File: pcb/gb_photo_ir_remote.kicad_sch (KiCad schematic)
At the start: 10 parts, among them SW1 SW_Push_SPDT, SW2 SW_Push_SPDT, U1 NE555P

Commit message: build
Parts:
- BT1: footprint Battery:BatteryHolder_Keystone_1060_1x2032 -> REB:REB_BatteryHolder_2032
- C1: footprint Capacitor_THT:C_Rect_L9.0mm_W3.4mm_P7.50mm_MKT -> Capacitor_THT:C_Disc_D5.0mm_W2.5mm_P2.50mm
- D1, D2: footprint LED_THT:LED_D5.0mm_Horizontal_O3.81mm_Z3.0mm -> LED_THT:LED_D5.0mm_Horizontal_O1.27mm_Z3.0mm
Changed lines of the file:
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@@
       (effects (font (size 1.27 1.27)) (justify left))
     )
-    (property "Footprint" "Battery:BatteryHolder_Keystone_1060_1x2032" (at 34.29 67.056 90)
+    (property "Footprint" "REB:REB_BatteryHolder_2032" (at 34.29 67.056 90)
       (effects (font (size 1.27 1.27)) hide)
     )
     (property "Datasheet" "~" (at 34.29 67.056 90)
       (effects (font (size 1.27 1.27)) hide)
+    )
+    (property "Notes" "" (at 34.29 68.58 0)
+      (effects (font (size 1.27 1.27)))
     )
     (pin "1")
@@
       (effects (font (size 1.27 1.27)) (justify left))
     )
-    (property "Footprint" "Capacitor_THT:C_Rect_L9.0mm_W3.4mm_P7.50mm_MKT" (at 62.23 88.9 0)
+    (property "Footprint" "Capacitor_THT:C_Disc_D5.0mm_W2.5mm_P2.50mm" (at 62.23 88.9 0)
       (effects (font (size 1.27 1.27)) hide)
     )
@@
       (effects (font (size 1.27 1.27)) hide)
     )
+    (property "Notes" "" (at 62.23 88.9 0)
+      (effects (font (size 1.27 1.27)))
+    )
     (pin "1")
     (pin "2")
@@
       (effects (font (size 1.27 1.27)))
     )
-    (property "Footprint" "LED_THT:LED_D5.0mm_Horizontal_O3.81mm_Z3.0mm" (at 123.19 62.23 0)
+    (property "Footprint" "LED_THT:LED_D5.0mm_Horizontal_O1.27mm_Z3.0mm" (at 123.19 62.23 0)
       (effects (font (size 1.27 1.27)) hide)
     )
@@
       (effects (font (size 1.27 1.27)))
     )
-    (property "Footprint" "LED_THT:LED_D5.0mm_Horizontal_O3.81mm_Z3.0mm" (at 123.19 35.56 0)
+    (property "Footprint" "LED_THT:LED_D5.0mm_Horizontal_O1.27mm_Z3.0mm" (at 123.19 35.56 0)
       (effects (font (size 1.27 1.27)) hide)
     )
@@
       (effects (font (size 1.27 1.27)) hide)
     )
-    (pin "1")
+    (property "Notes" "" (at 123.19 35.56 0)
+      (effects (font (size 1.27 1.27)))
+    )
+    (pin "1")

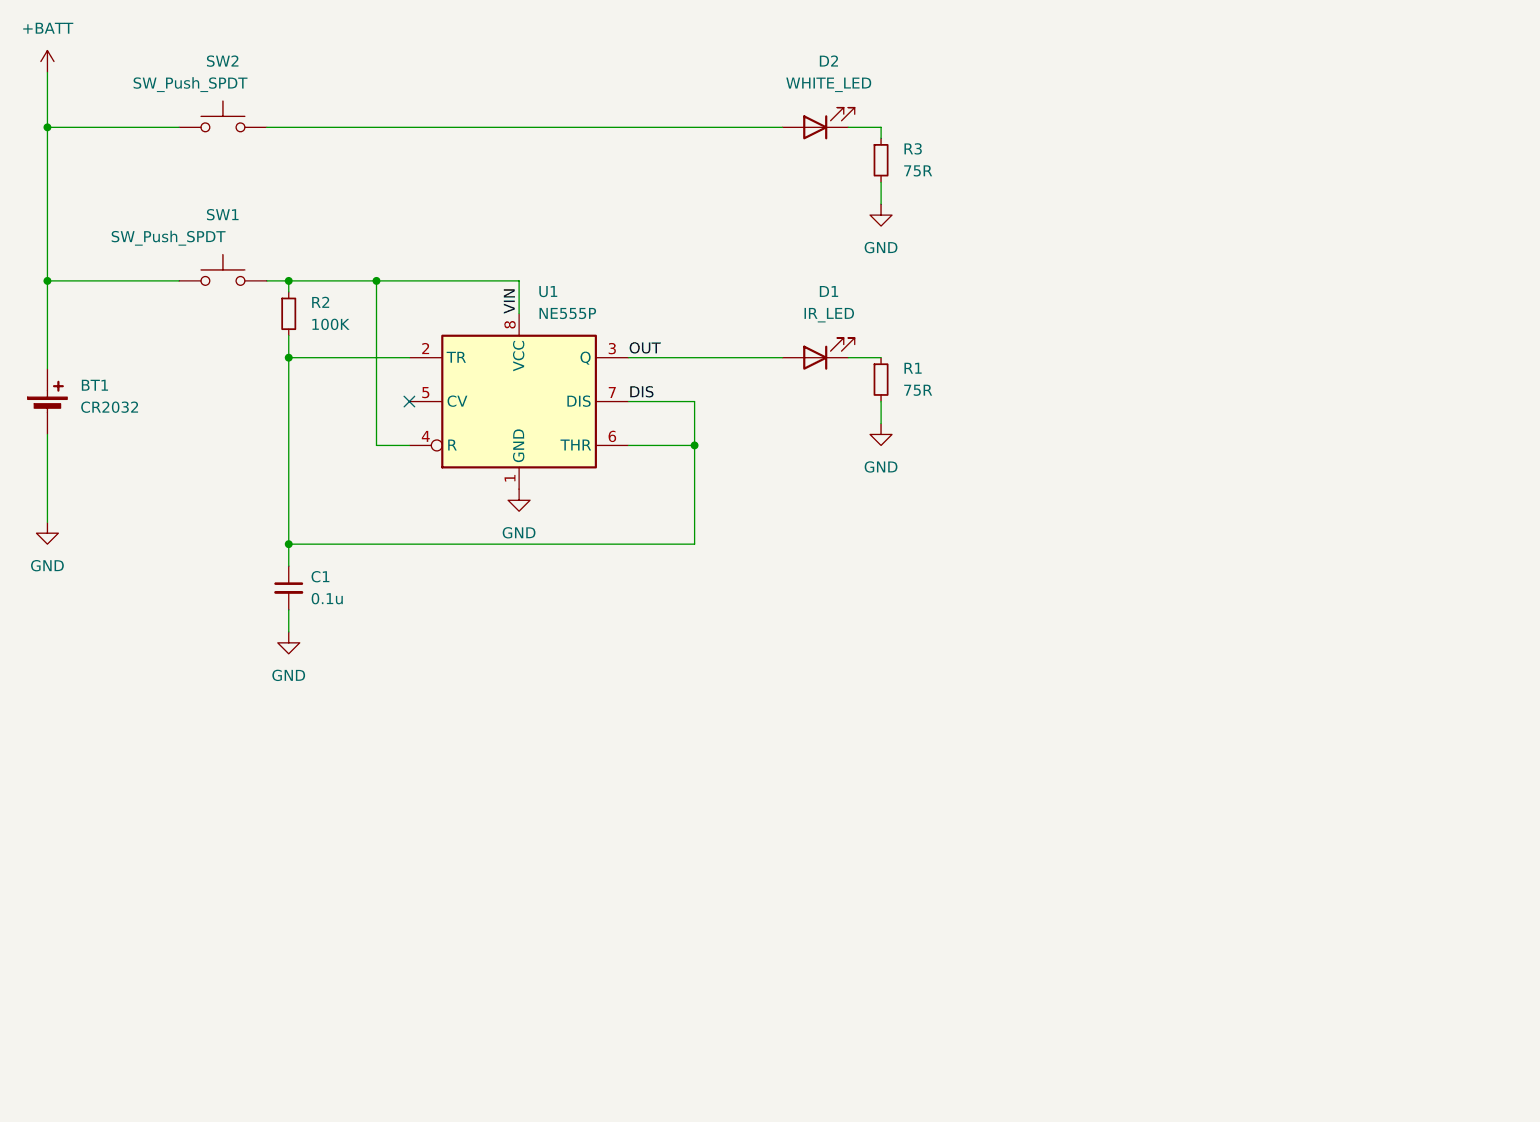
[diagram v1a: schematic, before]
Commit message: Timer didn't use an actual divider?
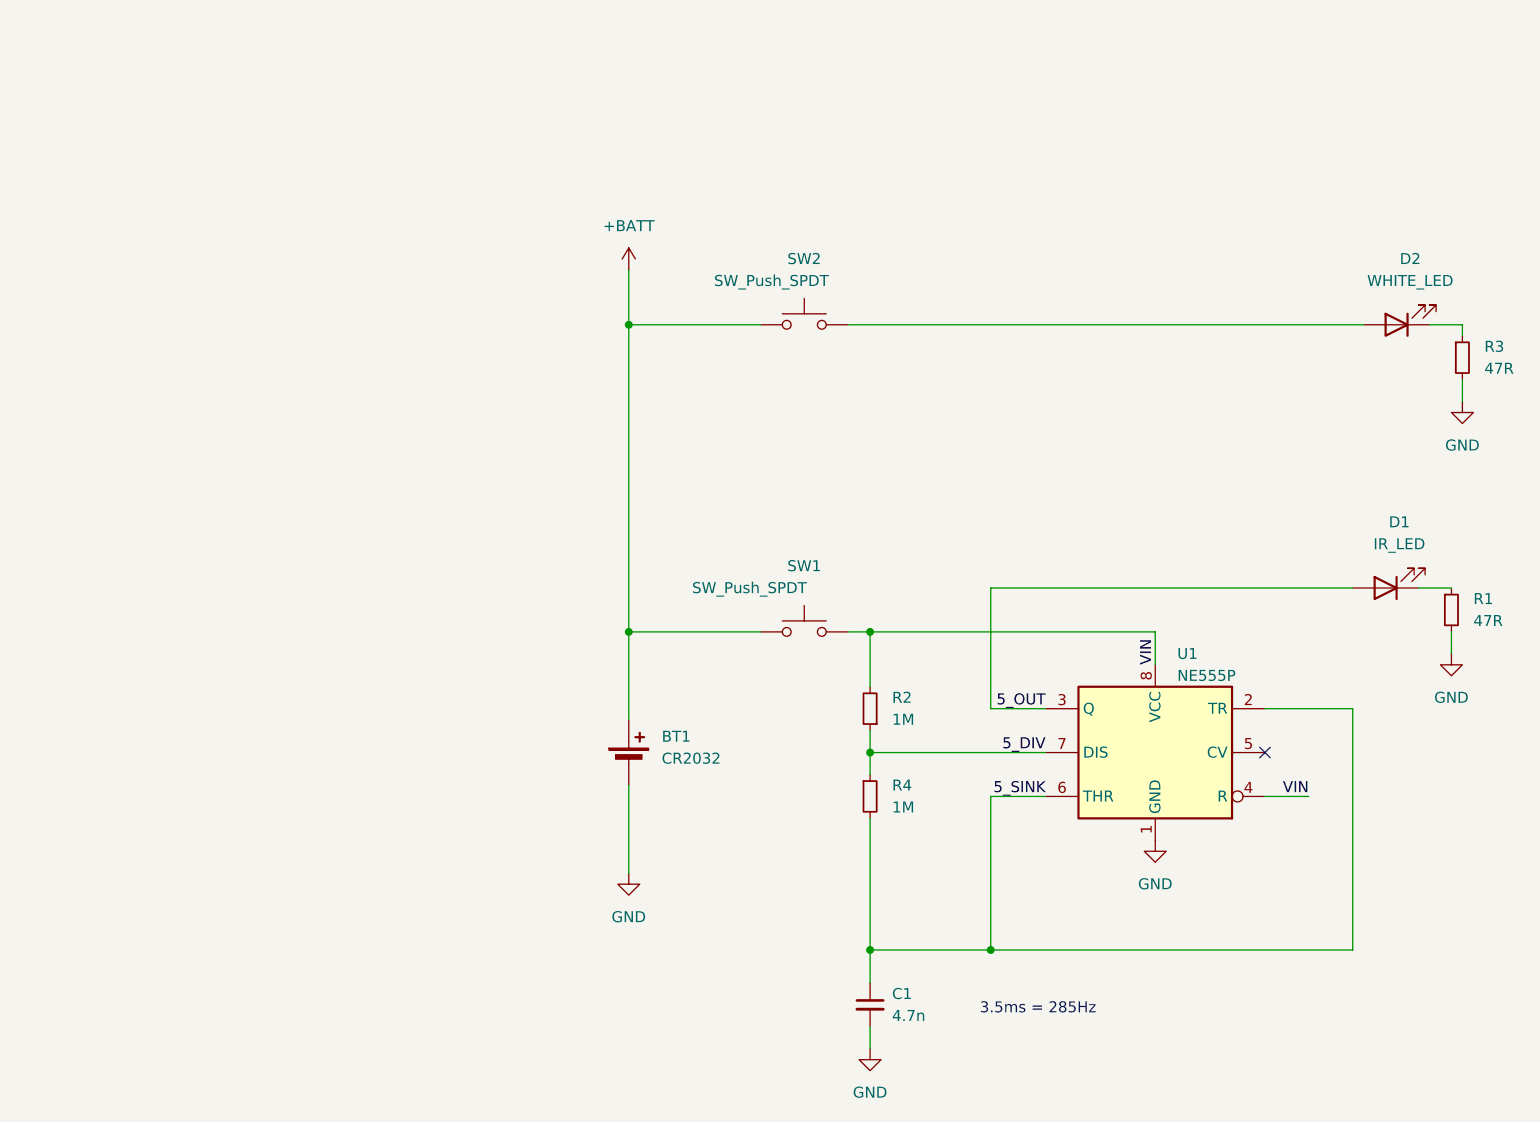
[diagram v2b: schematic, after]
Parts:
- added R4: 1M, Resistor_THT:R_Axial_DIN0207_L6.3mm_D2.5mm_P10.16mm_Horizontal, symbol Device:R_Small
- C1: value 0.1u -> 4.7n; footprint Capacitor_THT:C_Disc_D5.0mm_W2.5mm_P2.50mm -> Capacitor_THT:C_Disc_D5.0mm_W2.5mm_P5.00mm
- R1, R3: value 75R -> 47R
- R2: value 100K -> 1M
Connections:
- net VIN: now also R2.2; no longer R2.1
- net DIS renamed 5_SINK
- net 5_SINK: now also R4.2; no longer R2.2, U1.7 (DIS)
- net OUT renamed 5_OUT
- new net 5_DIV: R2.1, R4.1, U1.7 (DIS)
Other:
- note added: "3.5ms = 285Hz"
- moved on the sheet: BT1, C1, D1, D2, R1, R2, R3, SW1, SW2, U1
